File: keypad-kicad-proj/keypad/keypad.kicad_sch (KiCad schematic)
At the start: 3 parts, among them U1 ESP32-S3-WROOM-1

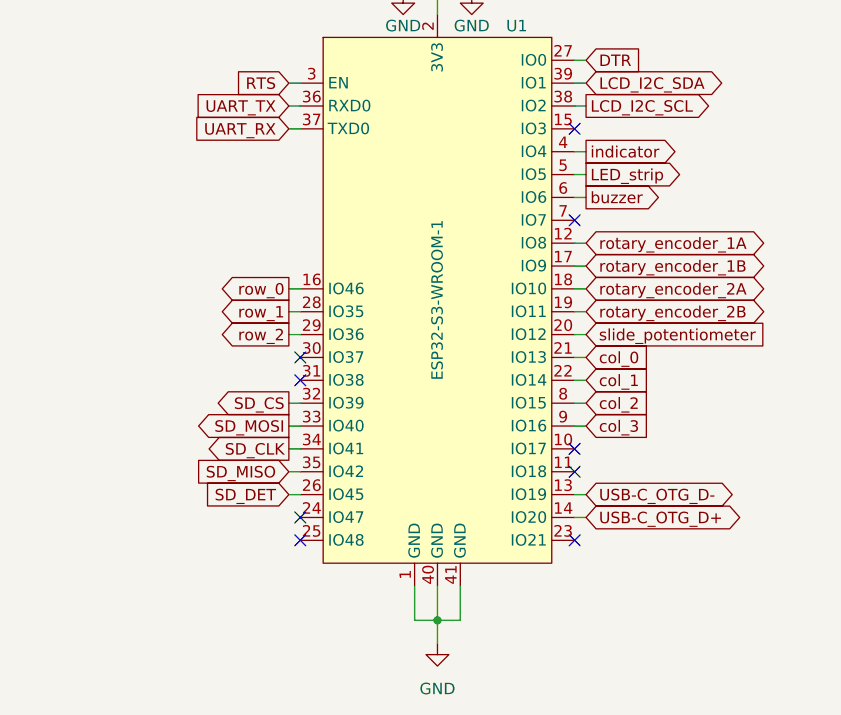
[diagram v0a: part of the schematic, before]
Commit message: assigned different pins so it's easier for the layout
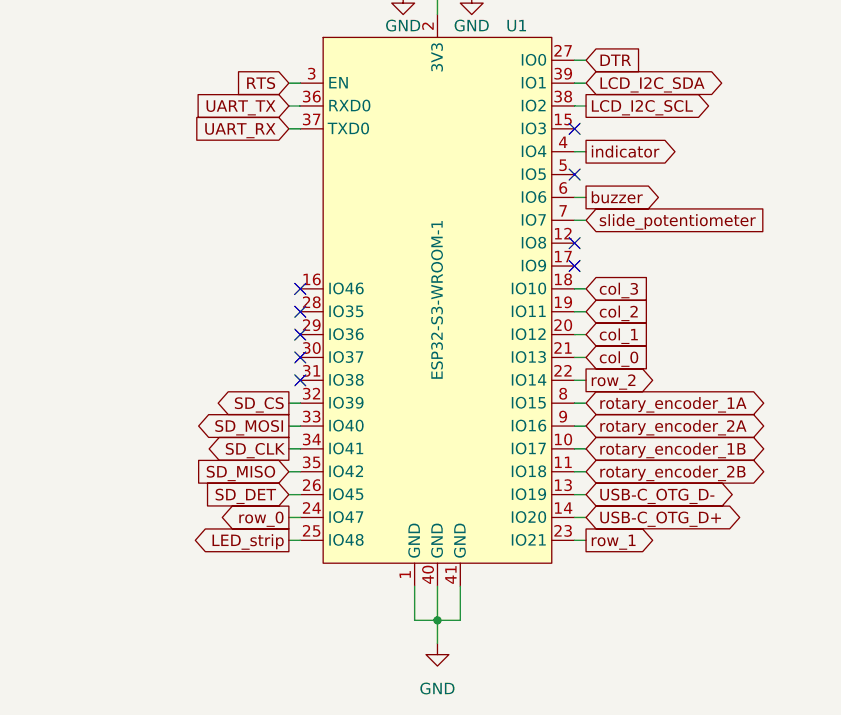
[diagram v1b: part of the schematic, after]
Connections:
- net LED_strip: now also U1.25 (IO48); no longer U1.5 (IO5)
- net col_1: now also U1.20 (IO12); no longer U1.22 (IO14)
- net col_2: now also U1.19 (IO11); no longer U1.8 (IO15)
- net col_3: now also U1.18 (IO10); no longer U1.9 (IO16)
- net rotary_encoder_1A: now also U1.8 (IO15); no longer U1.12 (IO8)
- net rotary_encoder_1B: now also U1.10 (IO17); no longer U1.17 (IO9)
- net rotary_encoder_2A: now also U1.9 (IO16); no longer U1.18 (IO10)
- net rotary_encoder_2B: now also U1.11 (IO18); no longer U1.19 (IO11)
- net row_0: now also U1.24 (IO47); no longer U1.16 (IO46)
- net row_1: now also U1.23 (IO21); no longer U1.28 (IO35)
- net row_2: now also U1.22 (IO14); no longer U1.29 (IO36)
- net slide_potentiometer: now also U1.7 (IO7); no longer U1.20 (IO12)

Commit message: layout update
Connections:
- net rotary_encoder_1A: now also U1.17 (IO9); no longer U1.8 (IO15)
- net rotary_encoder_1B: now also U1.16 (IO46); no longer U1.10 (IO17)
- net rotary_encoder_2A: now also U1.11 (IO18); no longer U1.9 (IO16)
- net rotary_encoder_2B: now also U1.10 (IO17); no longer U1.11 (IO18)
- net indicator: no longer names the net of U1.4 (IO4)
- no-connect marks 9 -> 10
